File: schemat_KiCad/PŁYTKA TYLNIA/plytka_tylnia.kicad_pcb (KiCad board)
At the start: 2 copper layers, 135 x 101 mm, 62 parts, among them J1 CONN_01X04, J2 PIN8, J3 PIN8, P1 USB_OTG

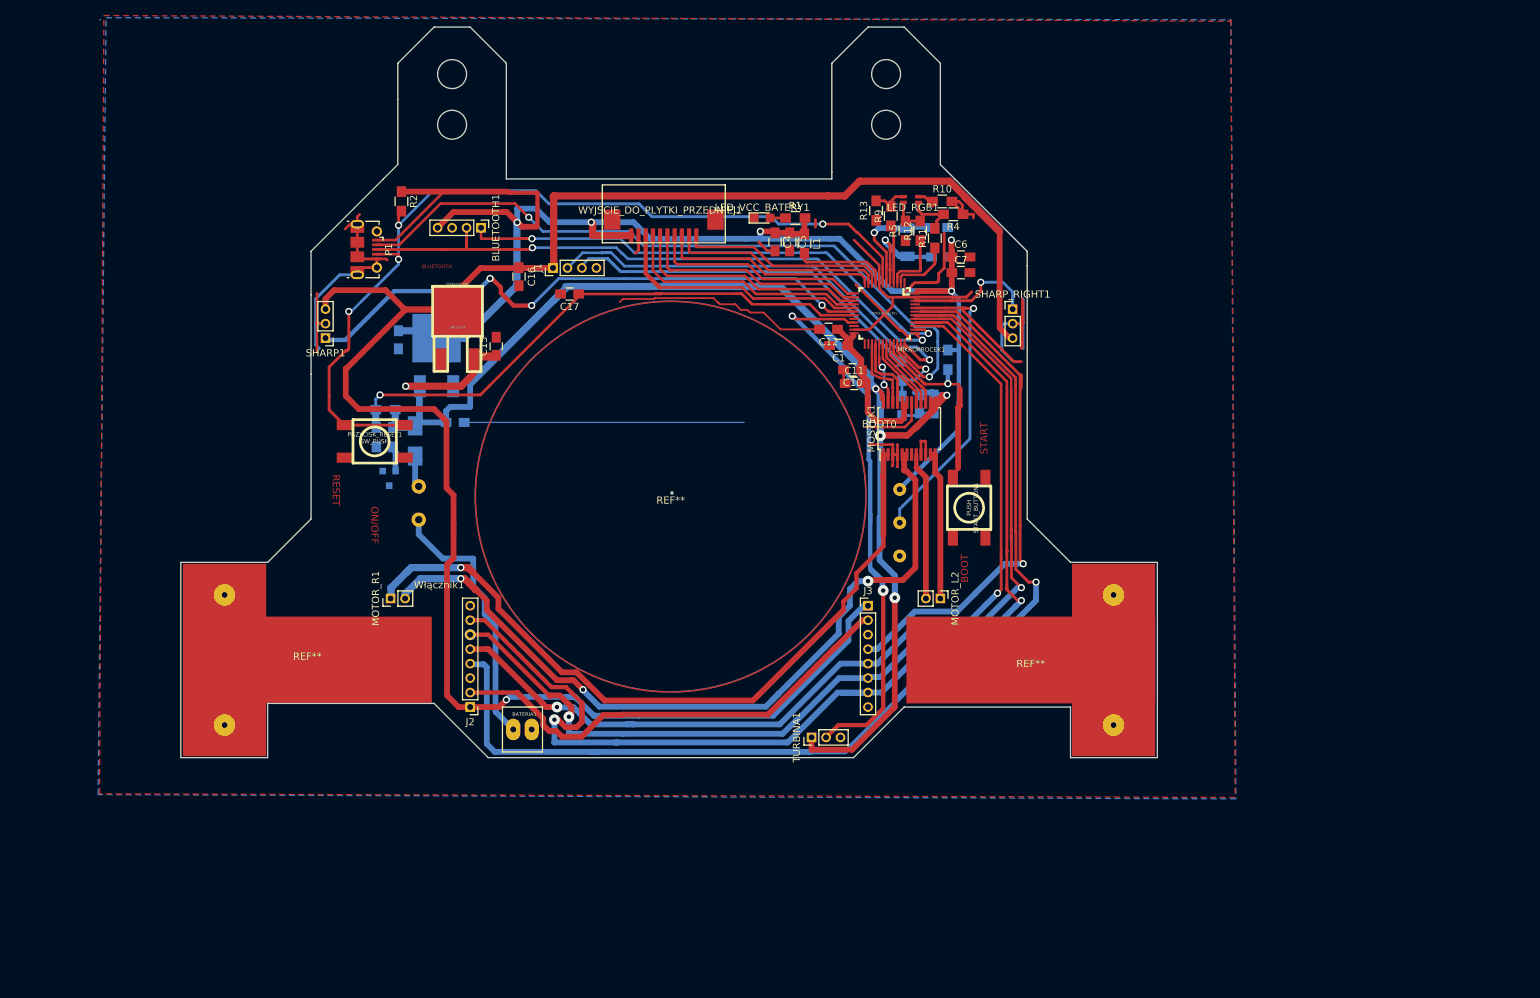
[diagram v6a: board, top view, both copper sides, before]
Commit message: zabezpieczenie przed odwrotną polaryzacją, ścieżki spi 0.6 , zwykle 0.4 zasilanie 1
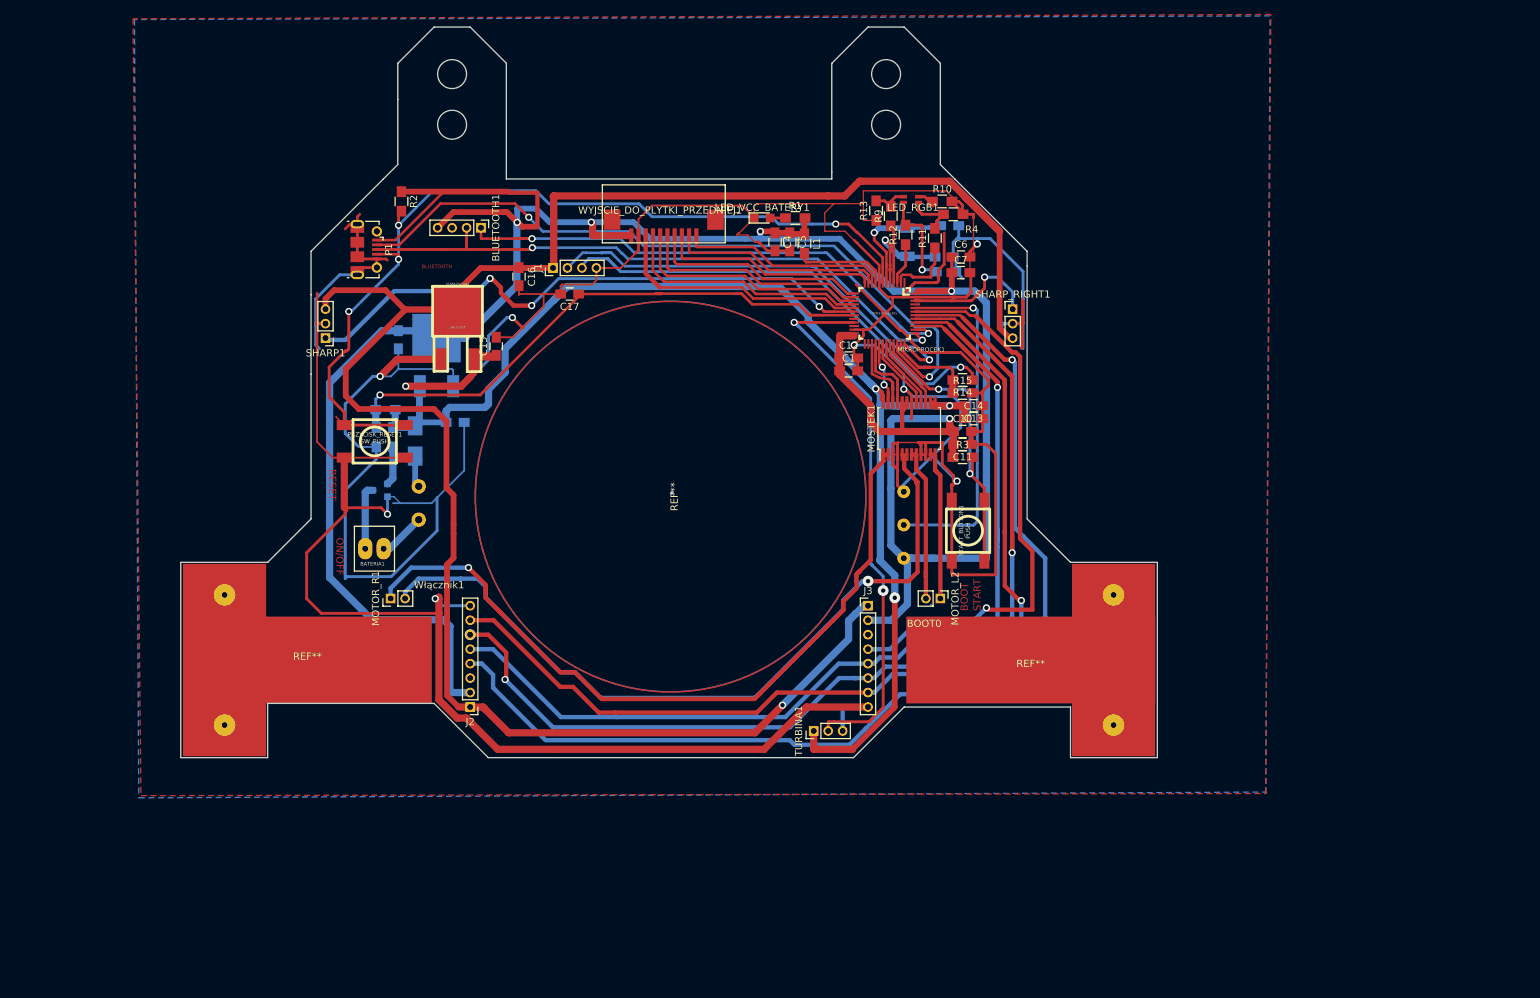
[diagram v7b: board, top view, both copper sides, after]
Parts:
- C13, C14, R14, R15, R3: moved to F.Cu
- R5: moved to B.Cu
- moved BATERIA1 32.1 mm to (94.0, 105.2), turned to 0 degrees
- moved C10 17.4 mm to (178.1, 85.9), turned to 0 degrees
- moved C11 17.2 mm to (178.1, 87.7), turned to 180 degrees
- moved R3 13.6 mm to (178.1, 89.5), turned to 0 degrees
- moved BOOT0 9.53 mm to (169.9, 103.4), turned to 180 degrees
- moved R15 8.57 mm to (178.1, 80.6), turned to 0 degrees
- moved R14 8.48 mm to (178.1, 78.8), turned to 180 degrees
- moved R5 7.95 mm to (175.8, 63.8), turned to 180 degrees
- moved C13 7.49 mm to (179.6, 82.4), turned to 180 degrees
- moved C14 5.80 mm to (179.6, 84.1), turned to 0 degrees
- moved C12 4.84 mm to (162.3, 75.7), turned to 0 degrees
- moved C1 3.77 mm to (162.3, 77.5), turned to 0 degrees
- moved START_BUTTON1 3.18 mm to (178.8, 99.6), turned to 90 degrees
- moved R12 2.09 mm to (170.2, 58.7)
- moved TRANSISTOR1 2.06 mm to (97.6, 94.0), turned to 90 degrees
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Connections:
- BATERIA1 pad 1: GND -> Net-(BATERIA1-Pad1)
- TRANSISTOR1 pad 1: GND -> Net-(R6-Pad2)
- TRANSISTOR1 pad 2: Net-(R6-Pad2) -> GND
- TRANSISTOR1 pad 3: GND -> Net-(BATERIA1-Pad1)
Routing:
- net GND: track 237.1 -> 711.4 mm, vias 0 -> 8
- net VCC: track 375.4 -> 451.4 mm
- net /SPI1_SS1: track 216.3 -> 148.3 mm
- net /BATERIA: track 278.2 -> 237.6 mm, vias 5 -> 4
- net Net-(BATERIA1-Pad2): track 42.7 -> 6.76 mm
- net /SPI1_SS2: track 72.4 -> 103.5 mm
- net /SPI1_MISO: track 162.8 -> 137.5 mm, vias 2 -> 1
- net Net-(MOSTEK1-Pad1): track 127.7 -> 104.6 mm
- net Net-(MIKROPROCEK1-Pad33): track 28.5 -> 43.1 mm, vias 1 -> 2
- net /ECHO: track 59.9 -> 73.4 mm, vias 0 -> 1
- net Net-(MOSTEK1-Pad5): track 120.2 -> 107.3 mm, vias 3 -> 1
- net /TURBINA_PWM: track 80.7 -> 93.0 mm
- net /5V: track 351.4 -> 340.6 mm
- net Net-(LED_RGB1-Pad3): track 4.72 -> 14.3 mm, vias 0 -> 1
- net /SPI1_CLK: track 140.8 -> 131.6 mm, vias 2 -> 1
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
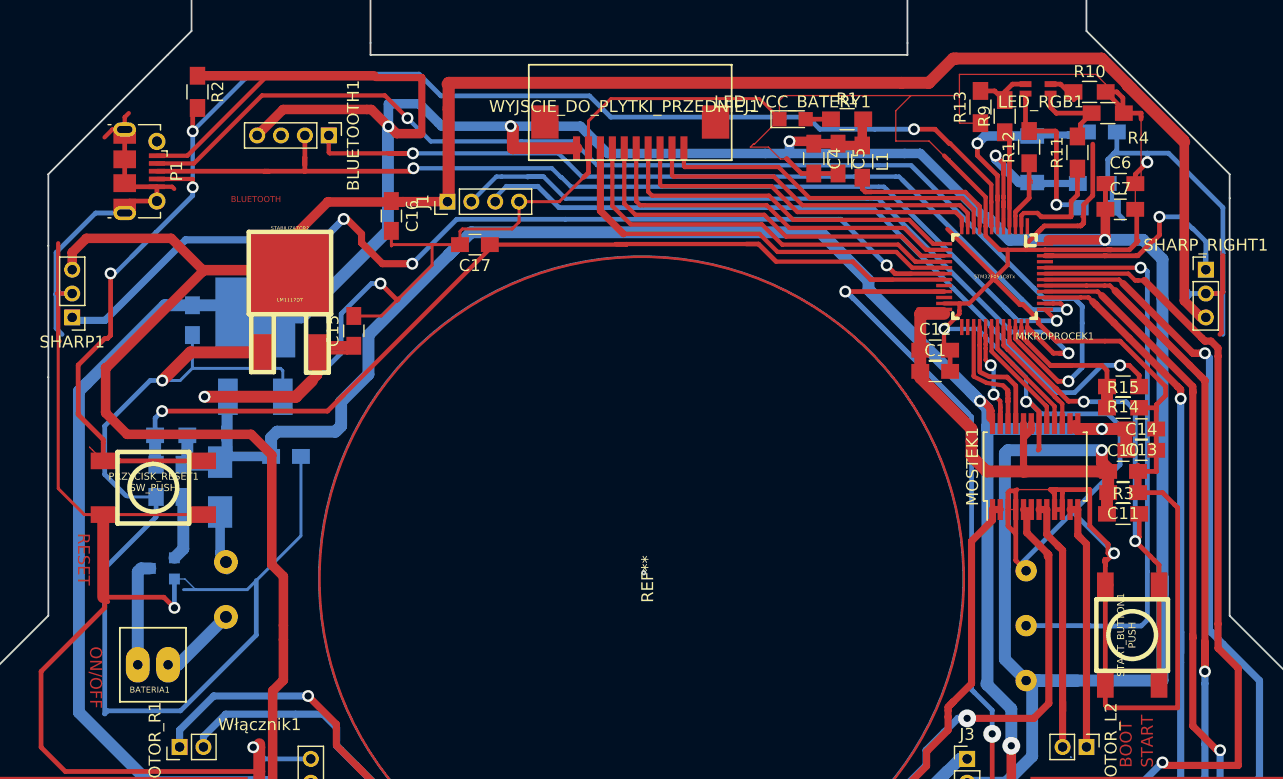
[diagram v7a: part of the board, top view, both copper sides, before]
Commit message: kondensatory spolaryzowane na tantalowe
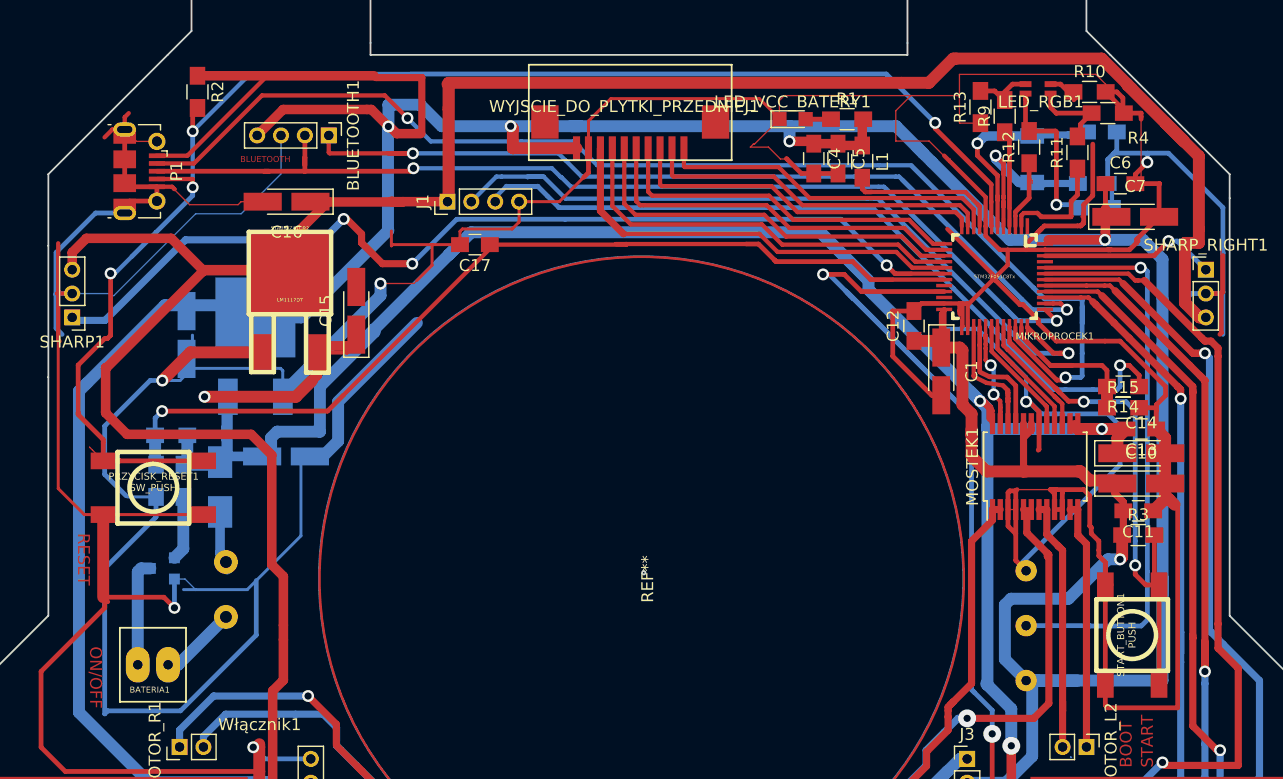
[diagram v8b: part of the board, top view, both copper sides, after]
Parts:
- C1, C10, C14, C15, C16, C7, C8, C9: footprint Capacitors_SMD:C_0805_HandSoldering -> Capacitors_Tantalum_SMD:CP_Tantalum_Case-A_EIA-3216-18_Hand
- moved C16 8.87 mm to (108.0, 63.3), turned to 180 degrees
- moved C12 2.70 mm to (160.5, 73.7), turned to 90 degrees
- moved R3 2.18 mm to (179.3, 91.2)
- moved C11 1.98 mm to (179.3, 89.2)
- moved C10 1.83 mm to (179.6, 86.9)
- moved C15 1.70 mm to (113.8, 72.4)
- moved C7 1.40 mm to (179.1, 64.6)
- moved C9 1.34 mm to (99.6, 74.5)
- moved C1 0.51 mm to (162.8, 77.5), turned to 270 degrees
- moved C14 0.25 mm to (179.6, 84.4)
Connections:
- MIKROPROCEK1 pad 25: (no net) -> GND
- MIKROPROCEK1 pad 26: (no net) -> GND
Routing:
- net GND: track 711.4 -> 766.2 mm, vias 8 -> 6
- net /5V: track 340.6 -> 347.0 mm
- net /SHARP_RIGHT: track 21.3 -> 15.0 mm
- net /TURBINA_PWM: track 93.0 -> 98.6 mm
- net /RESET: track 125.2 -> 130.4 mm
- net VCC: track 451.4 -> 448.2 mm
- net Net-(MIKROPROCEK1-Pad33): track 43.1 -> 45.7 mm
- net /BATERIA: track 237.6 -> 238.8 mm
- net /SWDIO: track 101.9 -> 102.9 mm
- net /ECHO: track 73.4 -> 74.2 mm
